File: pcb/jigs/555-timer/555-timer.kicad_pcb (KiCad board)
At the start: 2 copper layers, 16.5 x 15.5 mm, 17 parts, among them J1 Pin headers, J2 Pin headers, U1 NE555

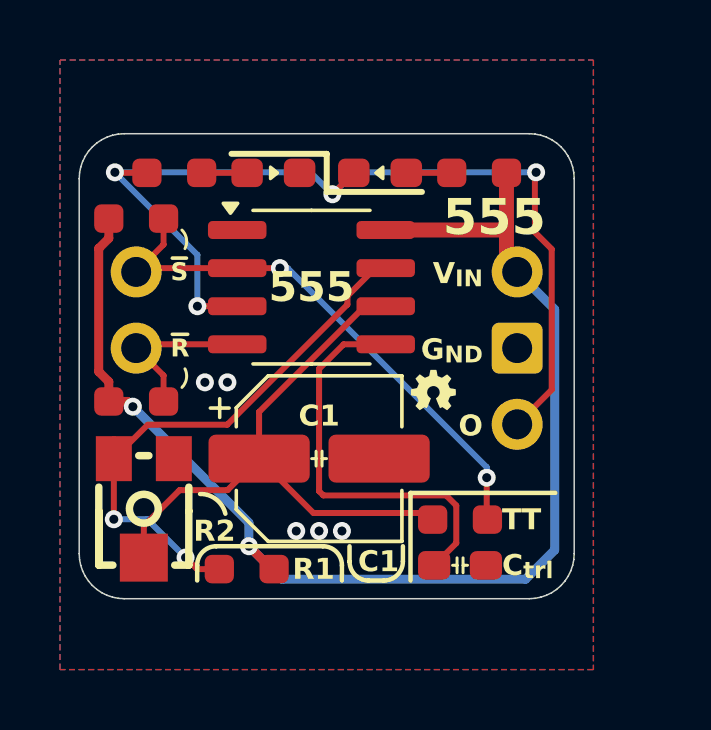
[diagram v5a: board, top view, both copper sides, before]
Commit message: Recreate potentiometer footprint in `discrete` footprint library
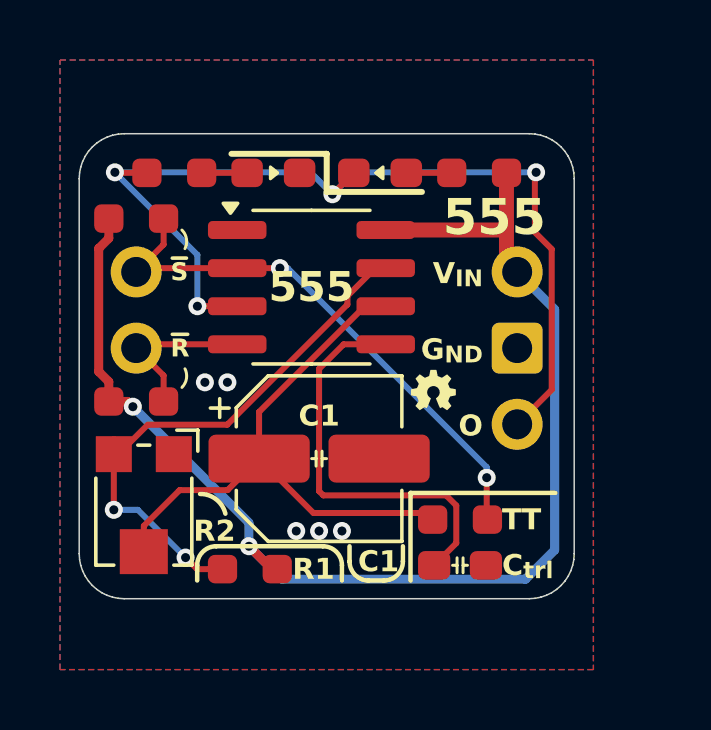
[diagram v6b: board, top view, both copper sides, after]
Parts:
- RV1: footprint lcsc:RES-ADJ-SMD_VG039NCH -> discrete:Potentiometer_3.8mmx3.0mm_Vertical
- moved R1 0.11 mm to (128.2, 93.7)
- turned RV1 to -90 degrees
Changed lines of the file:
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@@
 		)
 	)
-	(footprint "lcsc:RES-ADJ-SMD_VG039NCH"
+	(footprint "discrete:Potentiometer_3.8mmx3.0mm_Vertical"
 		(layer "F.Cu")
-		(at 124.714 91.694 90)
+		(at 124.714 91.694 -90)
+		(descr "Potentiometer, Bourns, TC33X, Vertical, https://www.bourns.com/pdfs/TC33.pdf")
+		(tags "Potentiometer Bourns TC33X Vertical")
 		(property "Reference" "RV1"
-			(at 0 -5 90)
+			(at 0 -2.5 90)
 			(layer "F.SilkS")
 			(hide yes)
@@
 		)
 		(property "Value" "500K"
-			(at 0 5 90)
+			(at 0 2.5 90)
 			(layer "F.Fab")
 			(effects
@@
 			)
 		)
-		(property "Footprint" "lcsc:RES-ADJ-SMD_VG039NCH"
-			(at 0 0 90)
+		(property "Footprint" "discrete:Potentiometer_3.8mmx3.0mm_Vertical"
+			(at 0 0 -90)
+			(unlocked yes)
 			(layer "F.Fab")
 			(hide yes)
@@
 		)
 		(property "Datasheet" ""
-			(at 0 0 90)
+			(at 0 0 -90)
+			(unlocked yes)
 			(layer "F.Fab")
 			(hide yes)
@@
 		)
 		(property "Description" "Potentiometer, US symbol"
-			(at 0 0 90)
+			(at 0 0 -90)
+			(unlocked yes)
 			(layer "F.Fab")
 			(hide yes)
@@
 		(attr smd)
 		(fp_line
-			(start -0.1 -1.5)
-			(end -1.9 -1.5)
+			(start -1 1.6)
+			(end 1.9 1.6)
 			(stroke
-				(width 0.25)
+				(width 0.12)
 				(type solid)
 			)
@@
 		)
 		(fp_line
-			(start -1.9 -1.5)
-			(end 0.7 -1.5)
+			(start 1.9 1.6)
+			(end 1.9 1)
 			(stroke
-				(width 0.25)
+				(width 0.12)
 				(type solid)
 			)
@@
 		)
 		(fp_line
-			(start -1.9 -1.03)
-			(end -1.9 -1.5)
+			(start -2.1 -0.2)
+			(end -2.1 0.2)
 			(stroke
-				(width 0.25)
+				(width 0.12)
 				(type solid)
 			)
@@
 		)
 		(fp_line
-			(start -1.9 -1.03)
-			(end -1.9 -1.5)
+			(start -1 -1.6)
+			(end 1.9 -1.6)
 			(stroke
-				(width 0.25)
+				(width 0.12)
 				(type solid)
 			)
@@
 		)
 		(fp_line
-			(start -1.9 -1.03)
-			(end -1.9 -1.5)
+			(start 1.9 -1.6)
+			(end 1.9 -1)
 			(stroke
-				(width 0.25)
+				(width 0.12)
 				(type solid)
 			)
@@
 		)
 		(fp_line
-			(start 1.75 0.17)
-			(end 1.75 -0.17)
+			(start -2.6 -1.8)
+			(end -2.6 -1.1)
 			(stroke
-				(width 0.25)
+				(width 0.12)
 				(type solid)
 			)
@@
 		)
 		(fp_line
-			(start -0.1 1.5)
-			(end 0.7 1.5)
+			(start -1.9 -1.8)
+			(end -2.6 -1.8)
 			(stroke
-				(width 0.25)
+				(width 0.12)
 				(type solid)
 			)
 			(layer "F.SilkS")
 		)
+		(fp_circle
+			(center 0 0)
+			(end 1.8 0)
+			(stroke
+				(width 0.05)
+				(type solid)
+			)
+			(fill none)
+			(layer "Dwgs.User")
+		)
 		(fp_line
-			(start -0.1 1.5)
-			(end -1.9 1.5)
+			(start -2.65 1.85)
+			(end -2.65 -1.85)
 			(stroke
-				(width 0.25)
+				(width 0.05)
 				(type solid)
 			)
-			(layer "F.SilkS")
+			(layer "F.CrtYd")
 		)
 		(fp_line
-			(start -1.9 1.5)
-			(end -1.9 1.03)
+			(start 2.45 1.85)
+			(end -2.65 1.85)
 			(stroke
-				(width 0.25)
+				(width 0.05)
 				(type solid)
 			)
-			(layer "F.SilkS")
+			(layer "F.CrtYd")
 		)
 		(fp_line
-			(start -1.9 1.5)
-			(end -1.9 1.03)
+			(start -2.65 -1.85)
+			(end 2.45 -1.85)
 			(stroke
-				(width 0.25)
+				(width 0.05)
 				(type solid)
 			)
-			(layer "F.SilkS")
+			(layer "F.CrtYd")
 		)
 		(fp_line
-			(start -1.9 1.5)
-			(end -1.9 1.03)
+			(start 2.45 -1.85)
+			(end 2.45 1.85)
 			(stroke
-				(width 0.25)
+				(width 0.05)
 				(type solid)
 			)
-			(layer "F.SilkS")
+			(layer "F.CrtYd")
 		)
-		(fp_circle
-			(center -0.02 0)
-			(end 0.46 0)
+		(fp_line
+			(start -2 1.5)
+			(end 1.8 1.5)
+			(stroke
+				(width 0.1)
+				(type solid)
+			)
+			(layer "F.Fab")
+		)
+		(fp_line
+			(start 1.8 1.5)
+			(end 1.8 -1.5)
 			(stroke
-				(width 0.25)
+				(width 0.1)
 				(type solid)
 			)
-			(fill none)
-			(layer "F.SilkS")
+			(layer "F.Fab")
 		)
-		(fp_circle
-			(center 2.1 1.2)
-			(end 2.2 1.2)
+		(fp_line
+			(start -2 -0.75)
+			(end -2 1.5)
 			(stroke
-				(width 0.2)
+				(width 0.1)
 				(type solid)
 			)
-			(fill none)
-			(layer "Cmts.User")
+			(layer "F.Fab")
+		)
+		(fp_line
+			(start -1.25 -1.5)
+			(end -2 -0.75)
+			(stroke
+				(width 0.1)
+				(type solid)
+			)
+			(layer "F.Fab")
+		)
+		(fp_line
+			(start 1.8 -1.5)
+			(end -1.25 -1.5)
+			(stroke
+				(width 0.1)
+				(type solid)
+			)
+			(layer "F.Fab")
 		)
 		(fp_circle
-			(center 1.9 1.5)
-			(end 1.93 1.5)
+			(center 0 0)
+			(end 1.5 0)
 			(stroke
-				(width 0.06)
+				(width 0.1)
 				(type solid)
 			)
@@
 			(layer "F.Fab")
 		)
+		(fp_text user "Wiper may be\nanywhere within\ncircle shown"
+			(at -0.15 -0.8 90)
+			(layer "Cmts.User")
+			(effects
+				(font
+					(size 0.15 0.15)
+					(thickness 0.02)
+				)
+			)
+		)
 		(fp_text user "${REFERENCE}"
 			(at 0 0 90)
@@
 			(effects
 				(font
-					(size 1 1)
-					(thickness 0.15)
+					(size 0.7 0.7)
+					(thickness 0.105)
 				)
 			)
 		)
 		(pad "1" smd rect
-			(at 1.65 1 180)
-			(size 1.2 1.5)
+			(at -1.8 -1 270)
+			(size 1.2 1.2)
 			(layers "F.Cu" "F.Paste" "F.Mask")
 			(net 11 "unconnected-(RV1-Pad1)")
@@
 		)
 		(pad "2" smd rect
-			(at -1.65 0 180)
-			(size 1.6 1.6)
+			(at 1.45 0 270)
+			(size 1.5 1.6)
 			(layers "F.Cu" "F.Paste" "F.Mask")
 			(net 3 "Net-(U1-Threshold)")
@@
 		)
 		(pad "3" smd rect
-			(at 1.65 -1 180)
-			(size 1.2 1.5)
+			(at -1.8 1 270)
+			(size 1.2 1.2)
 			(layers "F.Cu" "F.Paste" "F.Mask")
 			(net 4 "Net-(U1-Discharge)")
@@
 		(model "${KIPRJMOD}/libraries/lcsc.3dshapes/RES-ADJ-SMD_3P-L3.8-W3.0-H1.2-P1.90.wrl"
 			(offset
-				(xyz -0.09 -0 -0)
+				(xyz -0.1 0 0)
 			)
 			(scale
@@
 			)
 			(rotate
-				(xyz 0 0 270)
+				(xyz 0 0 90)
 			)
 		)
@@
 	(footprint "custom:R_0603_1608Metric_Pad0.98x0.95mm_HandSolder_simple"
 		(layer "F.Cu")
-		(at 128.143 93.726 180)
+		(at 128.25 93.726 180)
 		(descr "Resistor SMD 0603 (1608 Metric), square (rectangular) end terminal, IPC_7351 nominal with elongated pad for handsoldering. (Body size source: IPC-SM-782 page 72, https://www.pcb-3d.com/wordpress/wp-content/uploads/ipc-sm-782a_amendment_1_and_2.pdf), generated with kicad-footprint-generator")
 		(tags "resistor handsolder")
@@
 	)
 	(segment
+		(start 128.98 93.726)
+		(end 129.1625 93.726)
+		(width 0.3)
+		(layer "F.Cu")
+		(net 2)
+	)
+	(segment
 		(start 136.8025 82.25)
 		(end 136.8025 83.4625)
@@
 	)
 	(segment
+		(start 128.218 92.964)
+		(end 128.98 93.726)
+		(width 0.3)
+		(layer "F.Cu")
+		(net 2)
+	)
+	(segment
 		(start 136.8025 80.518)
 		(end 136.8025 82.25)
@@
 	)
 	(segment
-		(start 128.98 93.726)
-		(end 129.0555 93.726)
-		(width 0.3)
-		(layer "F.Cu")
-		(net 2)
-	)
-	(segment
 		(start 123.21 87.142)
 		(end 123.5475 87.4795)
@@
 	)
 	(segment
-		(start 128.218 92.964)
-		(end 128.98 93.726)
-		(width 0.3)
-		(layer "F.Cu")
-		(net 2)
-	)
-	(segment
 		(start 123.21 83.038)
 		(end 123.21 87.142)
@@
 	)
 	(segment
+		(start 127.3375 93.726)
+		(end 126.490002 93.726)
+		(width 0.2)
+		(layer "F.Cu")
+		(net 4)
+	)
+	(segment
 		(start 132.431448 83.693)
 		(end 132.777 83.693)
@@
 	)
 	(segment
-		(start 123.714 92.063763)
-		(end 123.714 90.044)
-		(width 0.2)
-		(layer "F.Cu")
-		(net 4)
-	)
-	(segment
 		(start 131.502 84.906)
 		(end 131.502 84.622448)
@@
 	)
 	(segment
-		(start 127.2305 93.726)
-		(end 126.490002 93.726)
+		(start 123.714 90.044)
+		(end 123.714 89.392)
 		(width 0.2)
 		(layer "F.Cu")
@@
 	)
 	(segment
-		(start 123.714 90.044)
-		(end 123.714 89.392)
+		(start 123.714 91.75)
+		(end 123.714 90.044)
 		(width 0.2)
 		(layer "F.Cu")
@@
 	)
 	(via
-		(at 123.714 92.063763)
+		(at 123.714 91.75)
 		(size 0.6)
 		(drill 0.3)
@@
 	)
 	(segment
-		(start 124.827765 92.063763)
+		(start 124.514002 91.75)
 		(end 126.105766 93.341764)
 		(width 0.2)
@@
 	)
 	(segment
-		(start 123.714 92.063763)
-		(end 124.827765 92.063763)
+		(start 123.714 91.75)
+		(end 124.514002 91.75)
 		(width 0.2)
 		(layer "B.Cu")

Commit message: Migrate 0603 capacitor hand soldering footprint to `discrete`
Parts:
- C0: footprint custom:C_0603_1608Metric_Pad1.08x0.95mm_HandSolder -> discrete:C_0603_1608Metric_Pad1.08x0.95mm_HandSolder
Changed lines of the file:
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@@
 	(net 10 "Net-(LED2-A)")
 	(net 11 "unconnected-(RV1-Pad1)")
-	(footprint "custom:C_0603_1608Metric_Pad1.08x0.95mm_HandSolder"
+	(footprint "discrete:C_0603_1608Metric_Pad1.08x0.95mm_HandSolder"
 		(layer "F.Cu")
 		(at 135.255 93.599)
@@
 			)
 		)
-		(property "Footprint" "custom:C_0603_1608Metric_Pad1.08x0.95mm_HandSolder"
+		(property "Footprint" "discrete:C_0603_1608Metric_Pad1.08x0.95mm_HandSolder"
 			(at 0 0 0)
 			(unlocked yes)

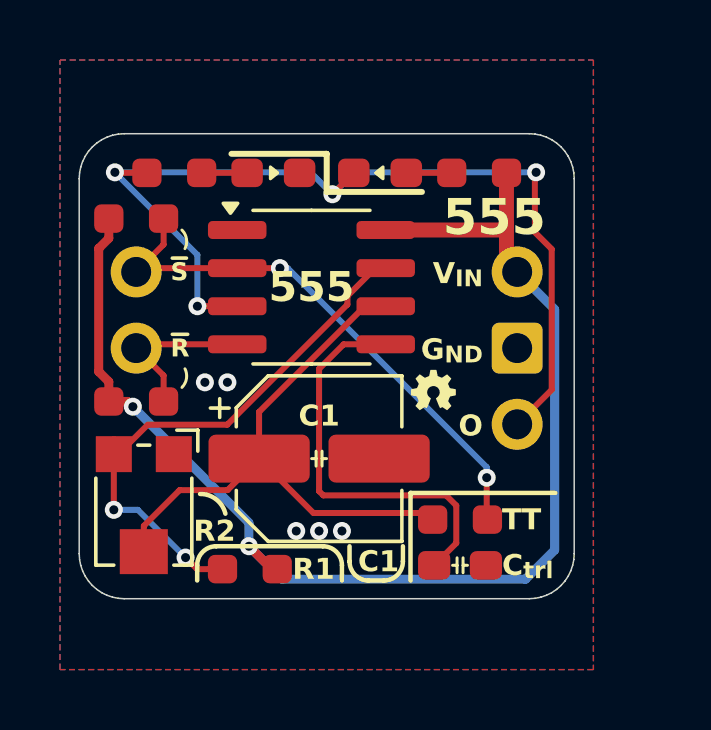
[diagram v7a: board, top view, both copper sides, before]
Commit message: Reduce custom footprint use on 555-timer
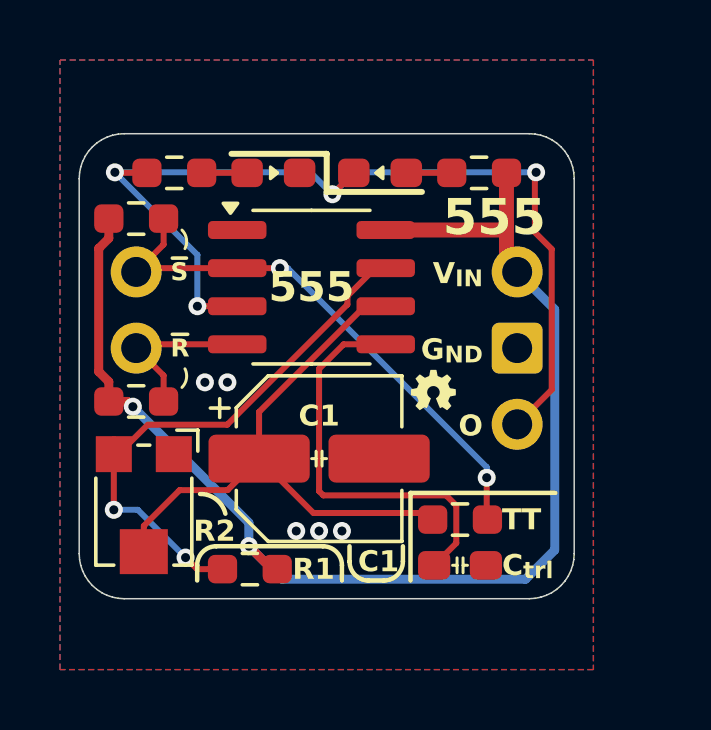
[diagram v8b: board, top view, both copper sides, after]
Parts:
- R0, R1, R3, R4, R5, R6: footprint custom:R_0603_1608Metric_Pad0.98x0.95mm_HandSolder_simple -> Resistor_SMD:R_0603_1608Metric_Pad0.98x0.95mm_HandSolder
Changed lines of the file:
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@@
 		)
 	)
-	(footprint "custom:R_0603_1608Metric_Pad0.98x0.95mm_HandSolder_simple"
+	(footprint "Resistor_SMD:R_0603_1608Metric_Pad0.98x0.95mm_HandSolder"
 		(layer "F.Cu")
 		(at 135.89 80.518 180)
@@
 			)
 		)
-		(property "Footprint" "custom:R_0603_1608Metric_Pad0.98x0.95mm_HandSolder_simple"
+		(property "Footprint" "Resistor_SMD:R_0603_1608Metric_Pad0.98x0.95mm_HandSolder"
 			(at 0 0 180)
 			(unlocked yes)
@@
 		(sheetfile "555-timer.kicad_sch")
 		(attr smd)
+		(fp_line
+			(start -0.254724 0.5225)
+			(end 0.254724 0.5225)
+			(stroke
+				(width 0.12)
+				(type solid)
+			)
+			(layer "F.SilkS")
+		)
+		(fp_line
+			(start -0.254724 -0.5225)
+			(end 0.254724 -0.5225)
+			(stroke
+				(width 0.12)
+				(type solid)
+			)
+			(layer "F.SilkS")
+		)
 		(fp_line
 			(start 1.65 0.73)
@@
 		)
 	)
-	(footprint "custom:R_0603_1608Metric_Pad0.98x0.95mm_HandSolder_simple"
+	(footprint "Resistor_SMD:R_0603_1608Metric_Pad0.98x0.95mm_HandSolder"
 		(layer "F.Cu")
 		(at 125.73 80.518)
@@
 		(tags "resistor handsolder")
 		(property "Reference" "R6"
-			(at 0 -1.43 180)
+			(at 0 -1.43 0)
 			(layer "F.SilkS")
 			(hide yes)
@@
 		)
 		(property "Value" "1K"
-			(at 0 1.43 180)
+			(at 0 1.43 0)
 			(layer "F.Fab")
 			(effects
@@
 			)
 		)
-		(property "Footprint" "custom:R_0603_1608Metric_Pad0.98x0.95mm_HandSolder_simple"
+		(property "Footprint" "Resistor_SMD:R_0603_1608Metric_Pad0.98x0.95mm_HandSolder"
 			(at 0 0 0)
 			(unlocked yes)
@@
 		(attr smd)
 		(fp_line
+			(start -0.254724 -0.5225)
+			(end 0.254724 -0.5225)
+			(stroke
+				(width 0.12)
+				(type solid)
+			)
+			(layer "F.SilkS")
+		)
+		(fp_line
+			(start -0.254724 0.5225)
+			(end 0.254724 0.5225)
+			(stroke
+				(width 0.12)
+				(type solid)
+			)
+			(layer "F.SilkS")
+		)
+		(fp_line
 			(start -1.65 -0.73)
 			(end 1.65 -0.73)
@@
 		)
 		(fp_text user "${REFERENCE}"
-			(at 0 0 180)
+			(at 0 0 0)
 			(layer "F.Fab")
 			(effects
@@
 		)
 	)
-	(footprint "custom:R_0603_1608Metric_Pad0.98x0.95mm_HandSolder_simple"
+	(footprint "Resistor_SMD:R_0603_1608Metric_Pad0.98x0.95mm_HandSolder"
 		(layer "F.Cu")
 		(at 124.46 88.138 180)
@@
 		(tags "resistor handsolder")
 		(property "Reference" "R0"
-			(at 0 -1.43 0)
+			(at 0 -1.43 180)
 			(layer "F.SilkS")
 			(hide yes)
@@
 		)
 		(property "Value" "0R"
-			(at 0 1.43 0)
+			(at 0 1.43 180)
 			(layer "F.Fab")
 			(effects
@@
 			)
 		)
-		(property "Footprint" "custom:R_0603_1608Metric_Pad0.98x0.95mm_HandSolder_simple"
+		(property "Footprint" "Resistor_SMD:R_0603_1608Metric_Pad0.98x0.95mm_HandSolder"
 			(at 0 0 180)
 			(unlocked yes)
@@
 		(attr smd)
 		(fp_line
+			(start -0.254724 0.5225)
+			(end 0.254724 0.5225)
+			(stroke
+				(width 0.12)
+				(type solid)
+			)
+			(layer "F.SilkS")
+		)
+		(fp_line
+			(start -0.254724 -0.5225)
+			(end 0.254724 -0.5225)
+			(stroke
+				(width 0.12)
+				(type solid)
+			)
+			(layer "F.SilkS")
+		)
+		(fp_line
 			(start 1.65 0.73)
 			(end -1.65 0.73)
@@
 		)
 		(fp_text user "${REFERENCE}"
-			(at 0 0 0)
+			(at 0 0 180)
 			(layer "F.Fab")
 			(effects
@@
 		)
 	)
-	(footprint "custom:R_0603_1608Metric_Pad0.98x0.95mm_HandSolder_simple"
+	(footprint "Resistor_SMD:R_0603_1608Metric_Pad0.98x0.95mm_HandSolder"
 		(layer "F.Cu")
 		(at 135.255 92.075 180)
@@
 			)
 		)
-		(property "Footprint" "custom:R_0603_1608Metric_Pad0.98x0.95mm_HandSolder_simple"
+		(property "Footprint" "Resistor_SMD:R_0603_1608Metric_Pad0.98x0.95mm_HandSolder"
 			(at 0 0 180)
 			(unlocked yes)
@@
 		(sheetfile "555-timer.kicad_sch")
 		(attr smd)
+		(fp_line
+			(start -0.254724 0.5225)
+			(end 0.254724 0.5225)
+			(stroke
+				(width 0.12)
+				(type solid)
+			)
+			(layer "F.SilkS")
+		)
+		(fp_line
+			(start -0.254724 -0.5225)
+			(end 0.254724 -0.5225)
+			(stroke
+				(width 0.12)
+				(type solid)
+			)
+			(layer "F.SilkS")
+		)
 		(fp_line
 			(start 1.65 0.73)
@@
 		)
 	)
-	(footprint "custom:R_0603_1608Metric_Pad0.98x0.95mm_HandSolder_simple"
+	(footprint "Resistor_SMD:R_0603_1608Metric_Pad0.98x0.95mm_HandSolder"
 		(layer "F.Cu")
 		(at 124.46 82.042 180)
@@
 		(tags "resistor handsolder")
 		(property "Reference" "R4"
-			(at 0 -1.43 0)
+			(at 0 -1.43 180)
 			(layer "F.SilkS")
 			(hide yes)
@@
 		)
 		(property "Value" "0R"
-			(at 0 1.43 0)
+			(at 0 1.43 180)
 			(layer "F.Fab")
 			(effects
@@
 			)
 		)
-		(property "Footprint" "custom:R_0603_1608Metric_Pad0.98x0.95mm_HandSolder_simple"
+		(property "Footprint" "Resistor_SMD:R_0603_1608Metric_Pad0.98x0.95mm_HandSolder"
 			(at 0 0 180)
 			(unlocked yes)
@@
 		(attr smd)
 		(fp_line
+			(start -0.254724 0.5225)
+			(end 0.254724 0.5225)
+			(stroke
+				(width 0.12)
+				(type solid)
+			)
+			(layer "F.SilkS")
+		)
+		(fp_line
+			(start -0.254724 -0.5225)
+			(end 0.254724 -0.5225)
+			(stroke
+				(width 0.12)
+				(type solid)
+			)
+			(layer "F.SilkS")
+		)
+		(fp_line
 			(start 1.65 0.73)
 			(end -1.65 0.73)
@@
 		)
 		(fp_text user "${REFERENCE}"
-			(at 0 0 0)
+			(at 0 0 180)
 			(layer "F.Fab")
 			(effects
@@
 		)
 	)
-	(footprint "custom:R_0603_1608Metric_Pad0.98x0.95mm_HandSolder_simple"
+	(footprint "Resistor_SMD:R_0603_1608Metric_Pad0.98x0.95mm_HandSolder"
 		(layer "F.Cu")
 		(at 128.25 93.726 180)
@@
 		(tags "resistor handsolder")
 		(property "Reference" "R1"
-			(at 0 -1.43 0)
+			(at 0 -1.43 180)
 			(layer "F.SilkS")
 			(hide yes)
@@
 		)
 		(property "Value" "10K"
-			(at 0 1.43 0)
+			(at 0 1.43 180)
 			(layer "F.Fab")
 			(effects
@@
 			)
 		)
-		(property "Footprint" "custom:R_0603_1608Metric_Pad0.98x0.95mm_HandSolder_simple"
+		(property "Footprint" "Resistor_SMD:R_0603_1608Metric_Pad0.98x0.95mm_HandSolder"
 			(at 0 0 180)
 			(unlocked yes)
@@
 		(attr smd)
 		(fp_line
+			(start -0.254724 0.5225)
+			(end 0.254724 0.5225)
+			(stroke
+				(width 0.12)
+				(type solid)
+			)
+			(layer "F.SilkS")
+		)
+		(fp_line
+			(start -0.254724 -0.5225)
+			(end 0.254724 -0.5225)
+			(stroke
+				(width 0.12)
+				(type solid)
+			)
+			(layer "F.SilkS")
+		)
+		(fp_line
 			(start 1.65 0.73)
 			(end -1.65 0.73)
@@
 		)
 		(fp_text user "${REFERENCE}"
-			(at 0 0 0)
-			(layer "F.Fab")
-			(effects
+			(at 0 0 180)
+			(layer "F.Fab")
+			(effects
